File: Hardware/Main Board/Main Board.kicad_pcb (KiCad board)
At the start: 4 copper layers, 71 x 57.5 mm, 85 parts, among them J1 Micro_SD_Card_Det1, J3 Conn_01x09_Socket, J4 MIC 1 Connector, J5 MIC 2 Connector, J6 USB_C_Receptacle_USB2.0_16P, J7 OLED, Q1 AO3401A, SW1 SW_SPST, U1 ESP32-S3-WROOM-2, U2 TPS63060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

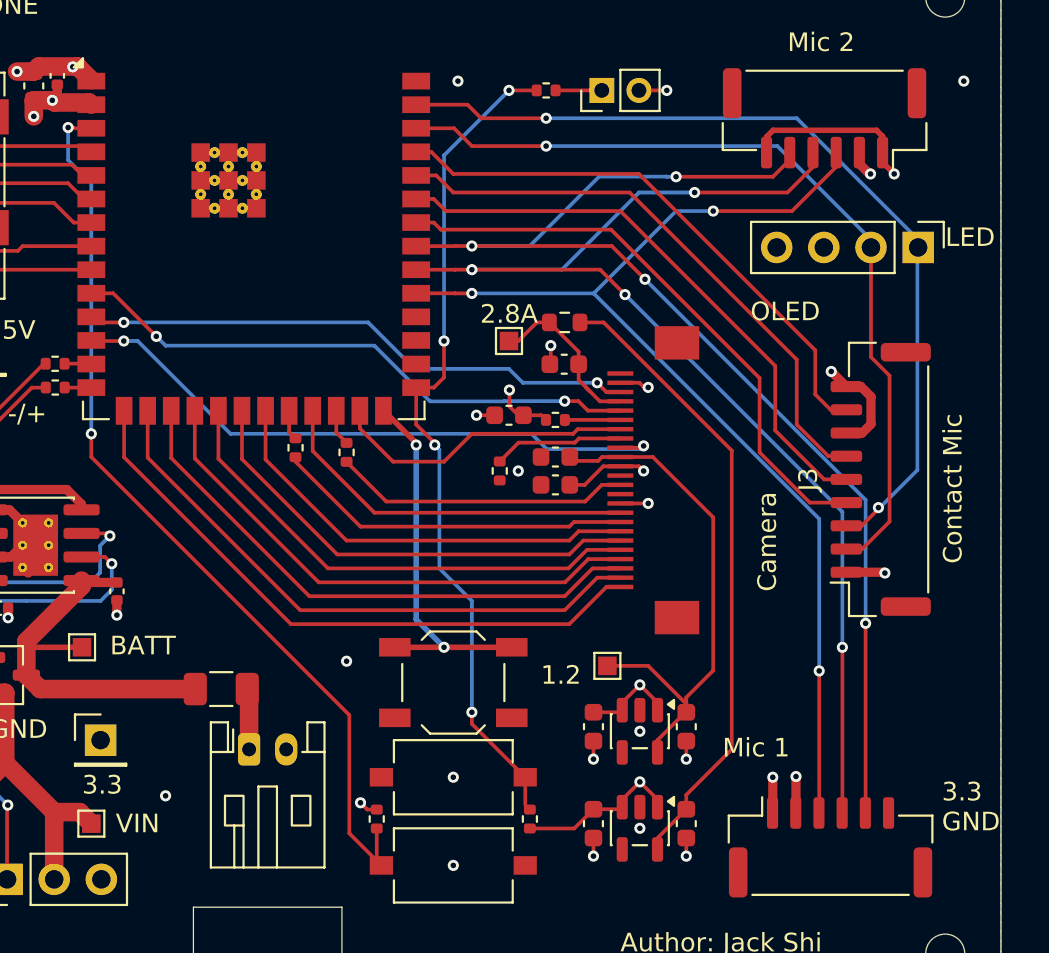
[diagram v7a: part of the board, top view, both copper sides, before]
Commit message: fixed data 0 and data 1 no connect issue, data pins for camera start at D2-D9
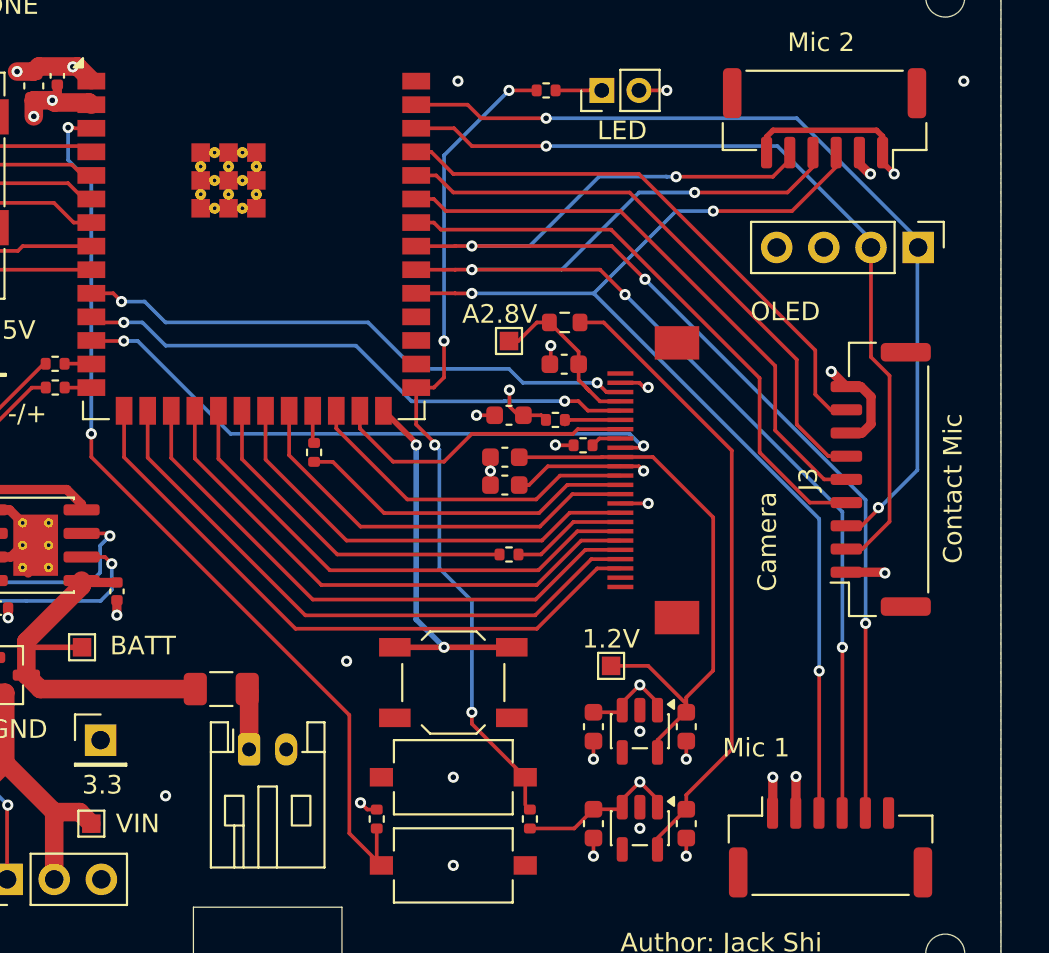
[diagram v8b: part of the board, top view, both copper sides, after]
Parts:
- removed 1.2, 2.8A: TestPoint, TestPoint:TestPoint_Pad_1.0x1.0mm
- added 1.2V: TestPoint, TestPoint:TestPoint_Pad_1.0x1.0mm, F.Cu at (123.5, 81.5)
- added A2.8V: TestPoint, TestPoint:TestPoint_Pad_1.0x1.0mm, F.Cu at (118.0, 64.0)
- moved R28 12.9 mm to (118.0, 75.5), turned to 0 degrees
- moved R27 4.70 mm to (122.0, 69.6), turned to 180 degrees
- moved C15 2.73 mm to (117.8, 70.3)
- moved C17 2.73 mm to (117.8, 71.8)
- moved R23 1.75 mm to (107.5, 70.0)
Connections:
- C14 pad 1: +3.3V -> Net-(CAM1-RESET)
- CAM1 pad 12: unconnected-(CAM1-DATA9-Pad12) -> CAM_D7
- CAM1 pad 14: unconnected-(CAM1-DATA8-Pad14) -> CAM_D6
- CAM1 pad 16: CAM_D7 -> CAM_D5
- CAM1 pad 18: CAM_D6 -> CAM_D4
- CAM1 pad 19: CAM_D2 -> CAM_D0
- CAM1 pad 20: CAM_D5 -> CAM_D3
- CAM1 pad 21: CAM_D3 -> CAM_D1
- CAM1 pad 22: CAM_D4 -> CAM_D2
- CAM1 pad 23: CAM_D1 -> unconnected-(CAM1-DATA1-Pad23)
- CAM1 pad 24: CAM_D0 -> unconnected-(CAM1-DATA0-Pad24)
- CAM1 pad 5: CAM_CLK -> CAM_SIO_CLK
- R23 pad 1: Net-(U1-IO47) -> Net-(U1-IO21)
- R28 pad 1: Net-(U1-IO14) -> Net-(U1-IO12)
- U1 pad 10: CAM_CLK -> CAM_SIO_DAT
- U1 pad 11: CAM_SIO_DAT -> CAM_SIO_CLK
- U1 pad 15: CAM_D0 -> CAM_D2
- U1 pad 17: CAM_D4 -> CAM_D3
- U1 pad 18: CAM_D3 -> CAM_D0
- U1 pad 19: CAM_D5 -> CAM_D4
- U1 pad 20: CAM_D2 -> Net-(U1-IO12)
- U1 pad 21: CAM_D6 -> CAM_D5
- U1 pad 22: Net-(U1-IO14) -> CAM_D6
- U1 pad 23: CAM_D7 -> Net-(U1-IO21)
- U1 pad 24: Net-(U1-IO47) -> CAM_D7
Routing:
- net CAM_CLK: track 31.1 -> 0.00 mm, vias 2 -> 0
- net CAM_SIO_CLK: track 0.00 -> 30.6 mm, vias 0 -> 2
- net Net-(U1-IO12): track 0.00 -> 18.6 mm
- net CAM_PCLK: track 19.3 -> 6.21 mm
- net CAM_D2: track 25.4 -> 34.4 mm
- net Net-(CAM1-PWDN): track 7.01 -> 1.65 mm
- net CAM_D0: track 33.8 -> 29.3 mm
- net CAM_D4: track 30.5 -> 27.6 mm
- net CAM_D5: track 27.1 -> 24.2 mm
- net +3.3V: track 62.0 -> 64.7 mm
- net 1.2V: track 28.8 -> 31.3 mm
- net CAM_D3: track 28.8 -> 31.1 mm
- net CAM_XCLK: track 16.0 -> 18.3 mm
- net Net-(U1-IO47): track 1.95 -> 0.00 mm
- net CAM_D7: track 20.1 -> 18.4 mm
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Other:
- board text removed: "3.3 GND"
